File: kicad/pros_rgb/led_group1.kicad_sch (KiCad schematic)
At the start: 7 parts

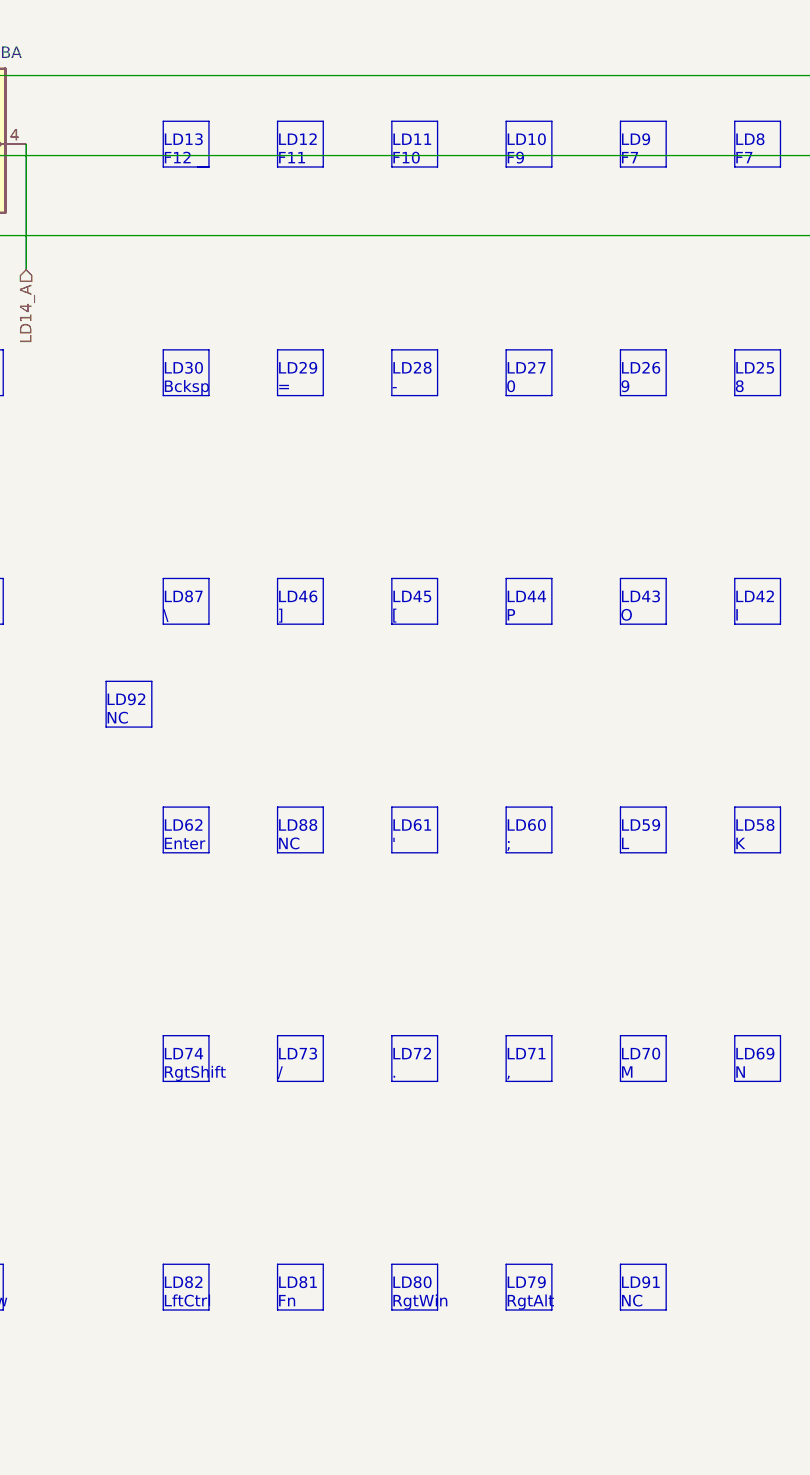
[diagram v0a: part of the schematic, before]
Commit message: kicad/pros_rgb: fix typos
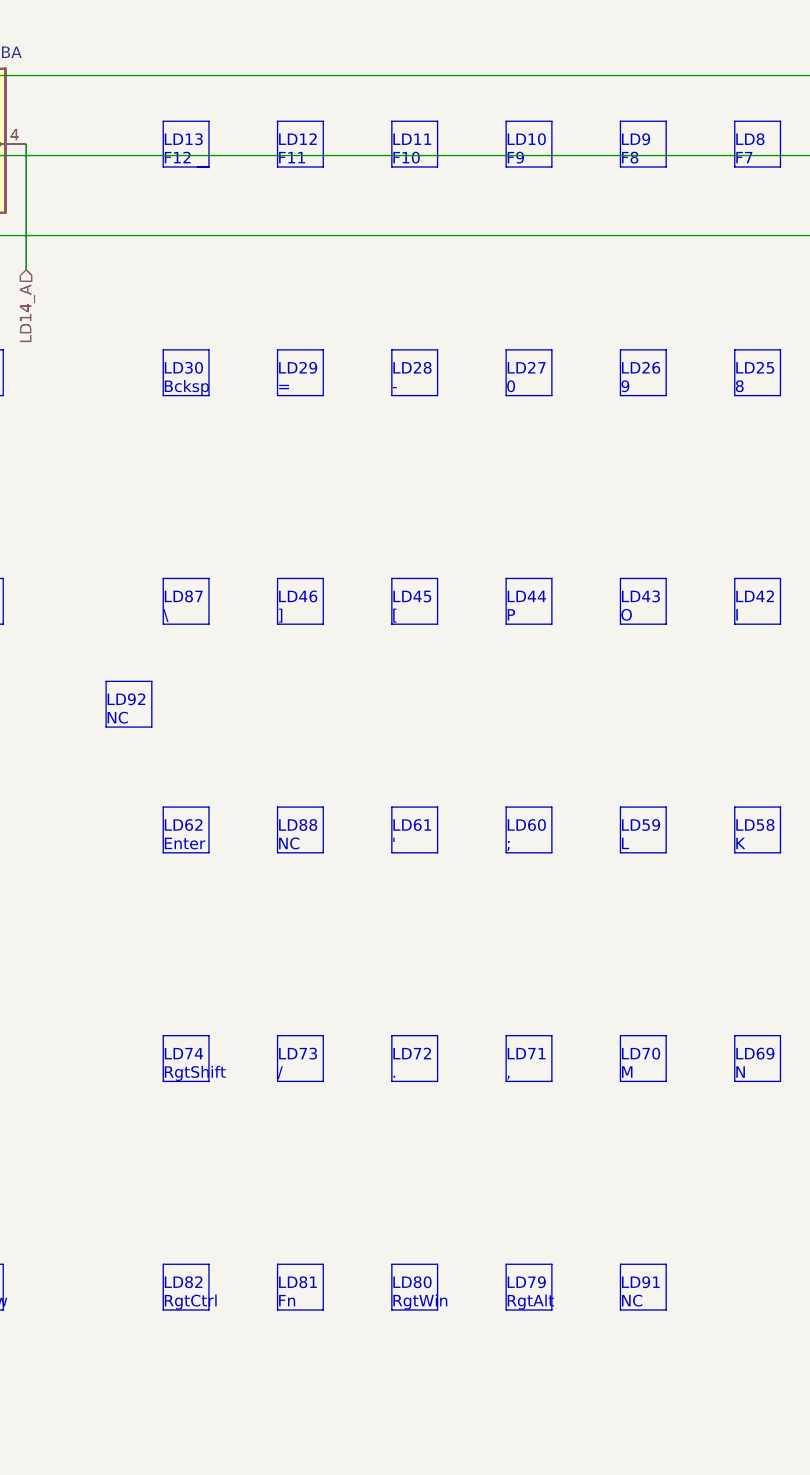
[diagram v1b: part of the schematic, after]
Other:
- note added: "LD82 RgtCtrl"
- note added: "LD9 F8"
- note removed: "LD82 LftCtrl"
- note removed: "LD9 F7"
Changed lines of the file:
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@@
     (effects (font (size 1.27 1.27)) (justify left bottom))
   )
-  (text "LD9\nF7" (at 157.48 29.21 0)
+  (text "LD9\nF8" (at 157.48 29.21 0)
     (effects (font (size 1.27 1.27)) (justify left bottom))
   )
@@
     (effects (font (size 1.27 1.27)) (justify left bottom))
   )
-  (text "LD82\nLftCtrl" (at 106.68 156.21 0)
+  (text "LD82\nRgtCtrl" (at 106.68 156.21 0)
     (effects (font (size 1.27 1.27)) (justify left bottom))
   )

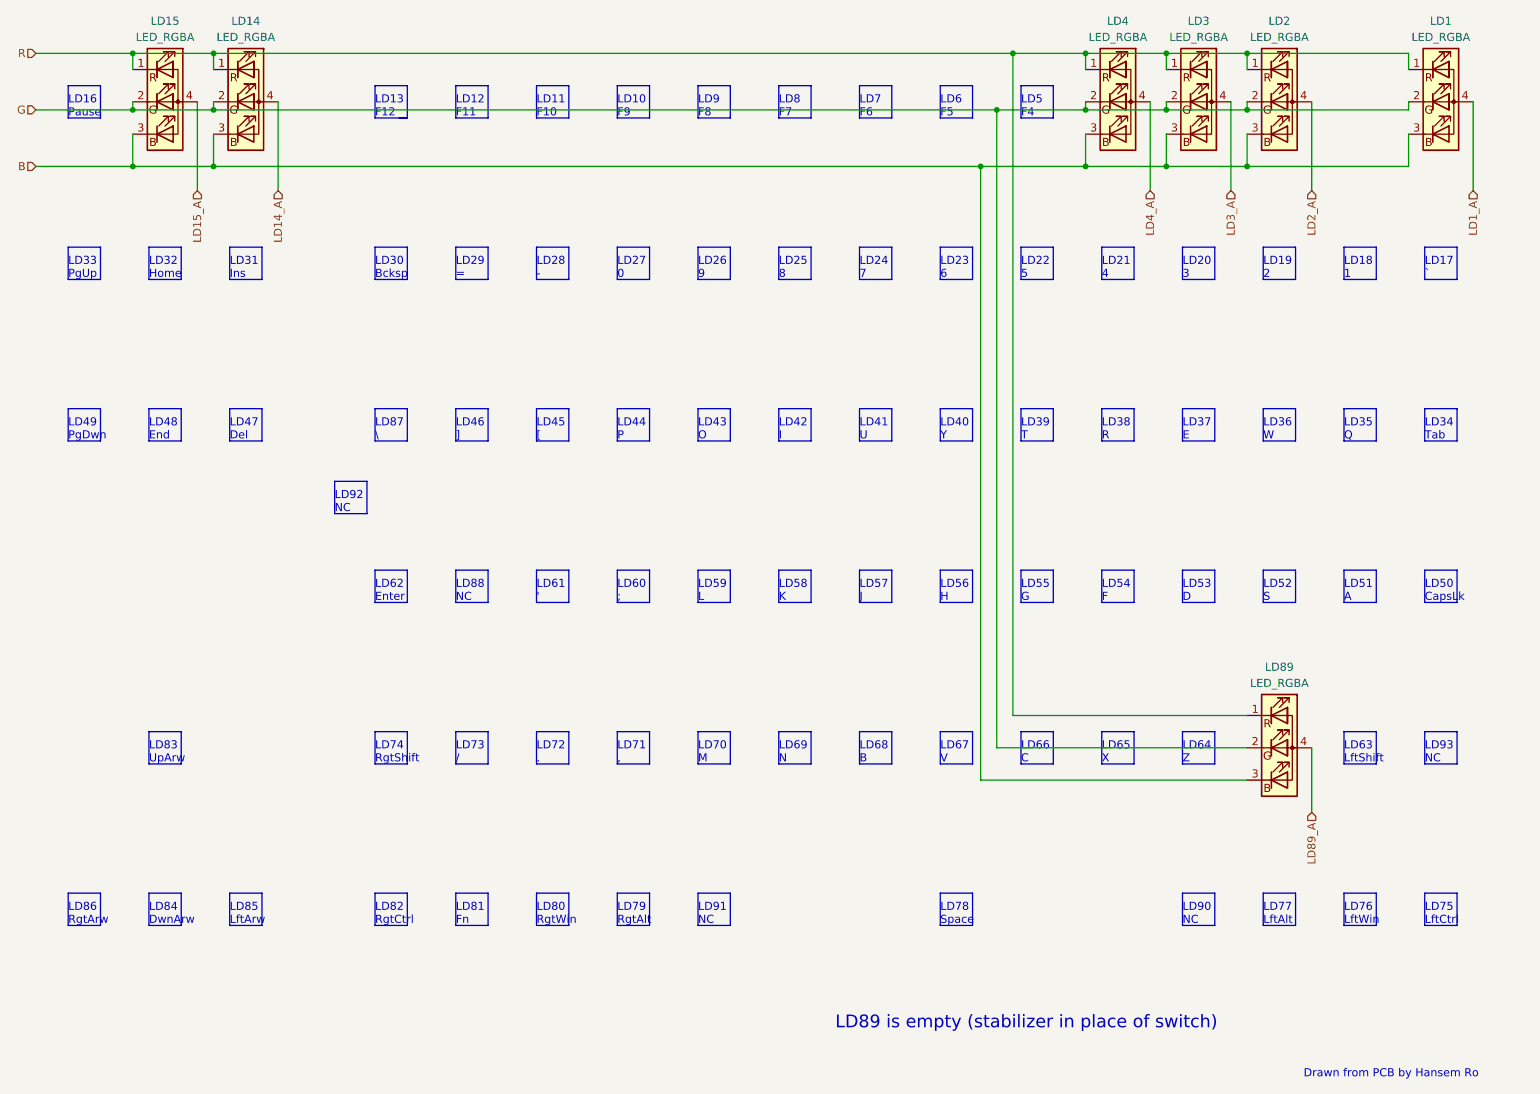
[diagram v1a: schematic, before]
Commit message: kicad/pros_rgb: order led groups by channel number
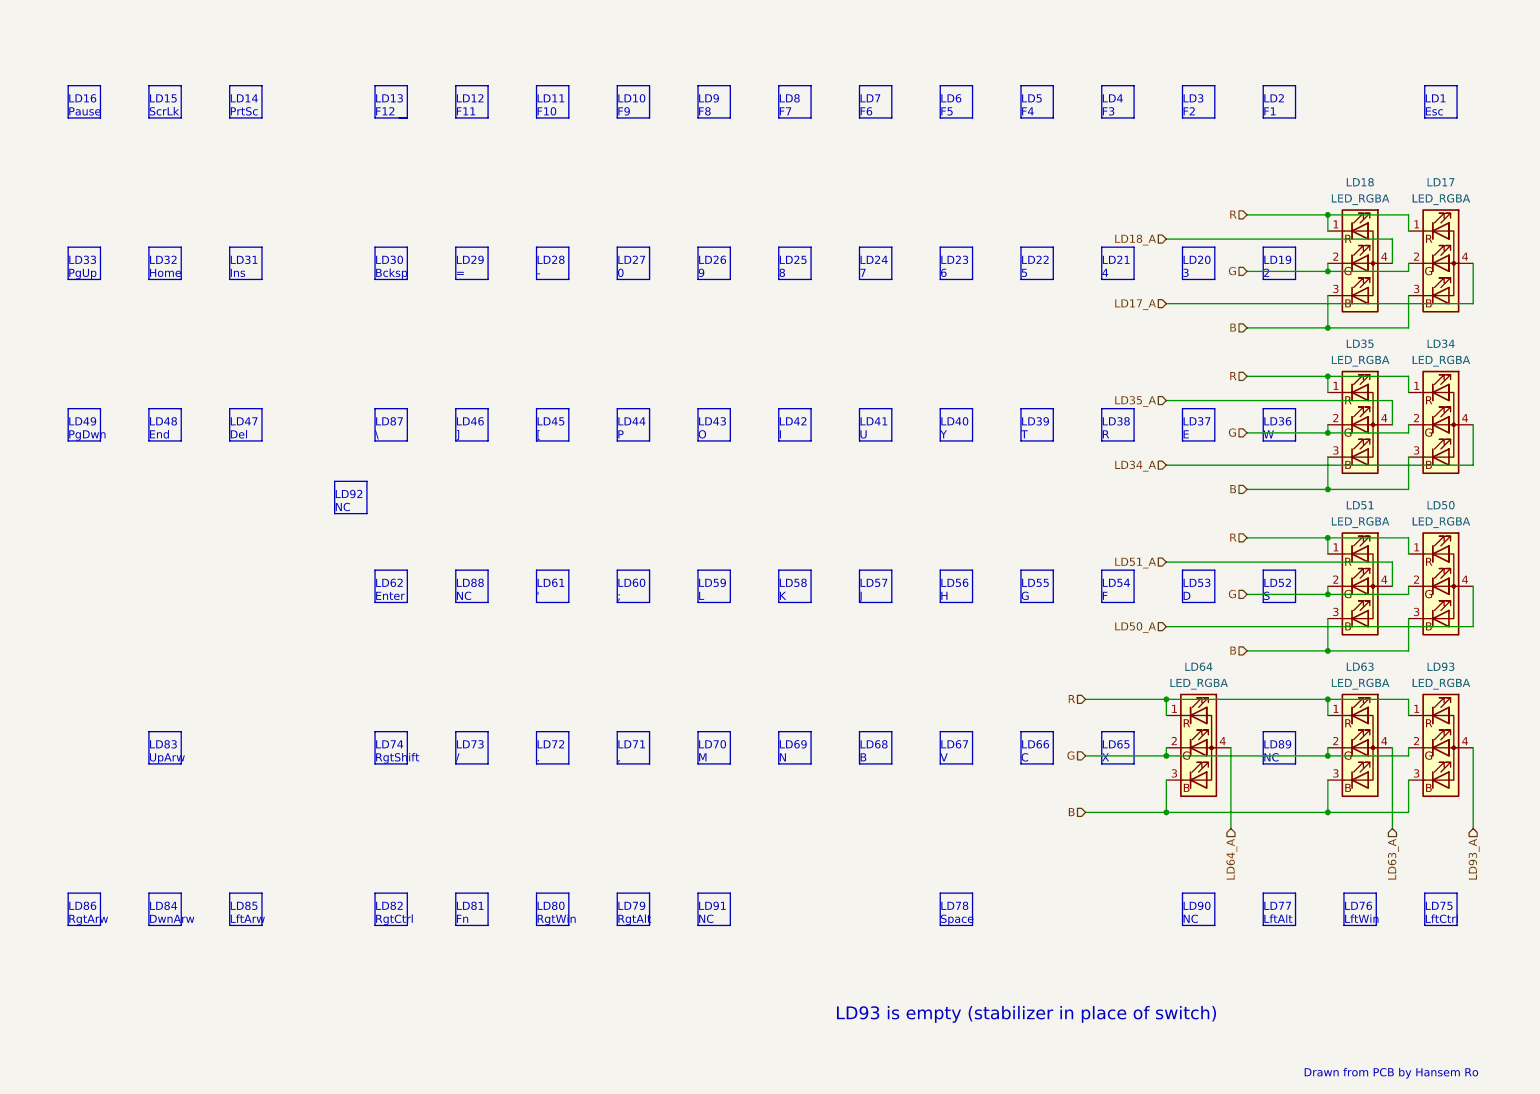
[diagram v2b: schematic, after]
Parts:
- removed LD1, LD14, LD15, LD2, LD3, LD4, LD89: LED_RGBA, symbol Device:LED_RGBA
- added LD17, LD18, LD34, LD35, LD50, LD51, LD63, LD64, LD93: LED_RGBA, symbol Device:LED_RGBA
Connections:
- net B: now also LD17.3 (BK), LD18.3 (BK), LD34.3 (BK), LD35.3 (BK), LD50.3 (BK), LD51.3 (BK), LD63.3 (BK), LD64.3 (BK), LD93.3 (BK)
- net G: now also LD17.2 (GK), LD18.2 (GK), LD34.2 (GK), LD35.2 (GK), LD50.2 (GK), LD51.2 (GK), LD63.2 (GK), LD64.2 (GK), LD93.2 (GK)
- net R: now also LD17.1 (RK), LD18.1 (RK), LD34.1 (RK), LD35.1 (RK), LD50.1 (RK), LD51.1 (RK), LD63.1 (RK), LD64.1 (RK), LD93.1 (RK)
- new net LD17_A: LD17.4 (A)
- new net LD18_A: LD18.4 (A)
- new net LD34_A: LD34.4 (A)
- new net LD35_A: LD35.4 (A)
- new net LD50_A: LD50.4 (A)
- new net LD51_A: LD51.4 (A)
- new net LD63_A: LD63.4 (A)
- new net LD64_A: LD64.4 (A)
- new net LD93_A: LD93.4 (A)
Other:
- note added: "LD1 Esc"
- note added: "LD14 PrtSc"
- note added: "LD15 ScrLk"
- note added: "LD2 F1"
- note added: "LD3 F2"
- note added: "LD4 F3"
- note added: "LD89 NC"
- note added: "LD93 is empty (stabilizer in place of switch)"
- note removed: "LD17 `"
- note removed: "LD18 1"
- note removed: "LD34 Tab"
- note removed: "LD35 Q"
- note removed: "LD50 CapsLk"
- note removed: "LD51 A"
- note removed: "LD63 LftShift"
- note removed: "LD64 Z"
- note removed: "LD89 is empty (stabilizer in place of switch)"
- note removed: "LD93 NC"
